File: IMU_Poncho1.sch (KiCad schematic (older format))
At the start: 9 parts, among them J1 Conn_01x06, J2 Conn_01x06_Female, U1 IMU9250

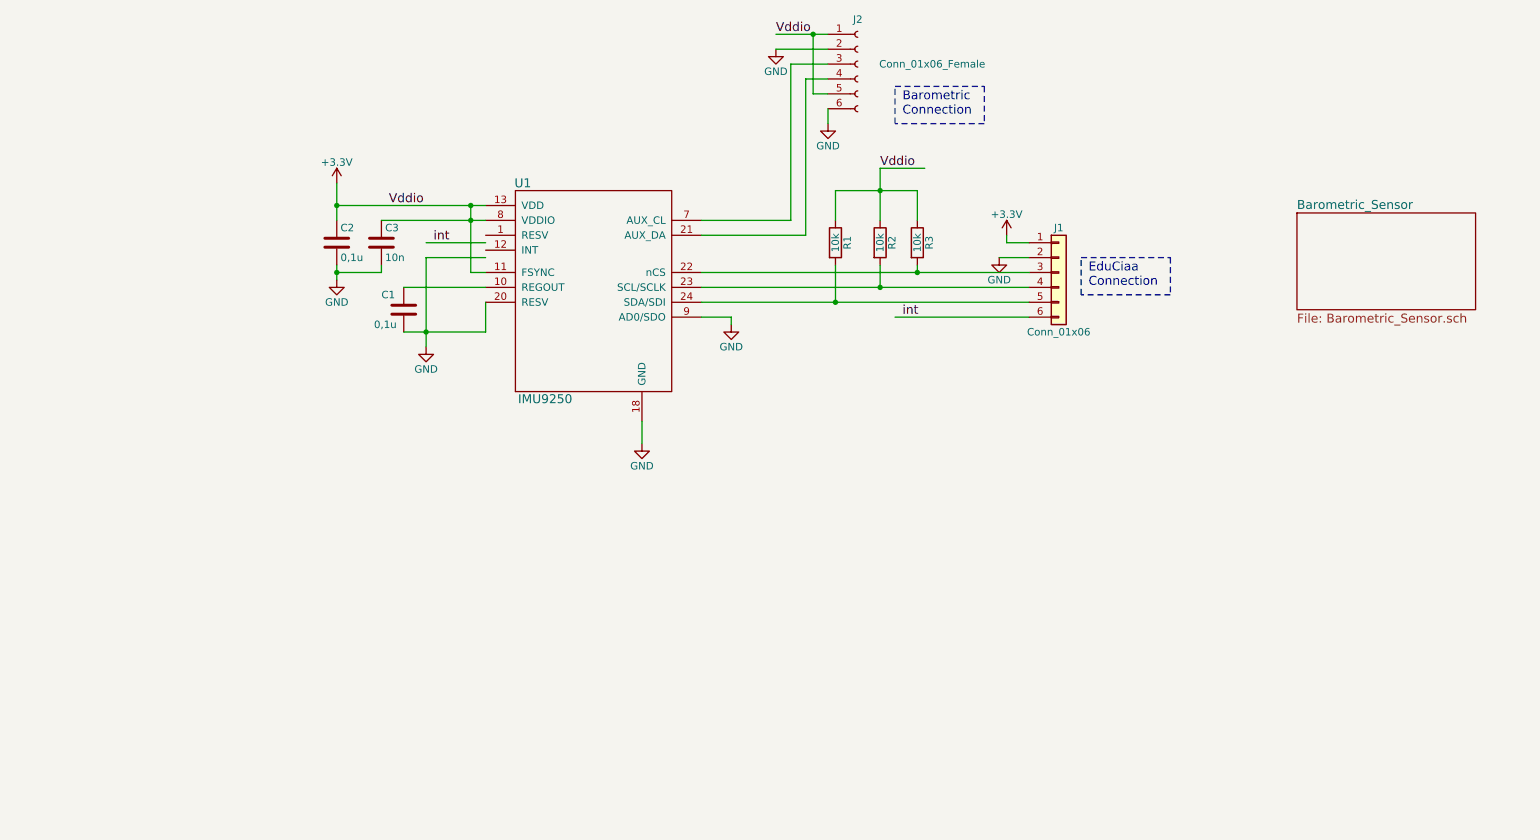
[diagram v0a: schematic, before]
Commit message: Corrigiendo esquematico + datasheets
Detalles de lineas y pines para que no se crucen, +pwr
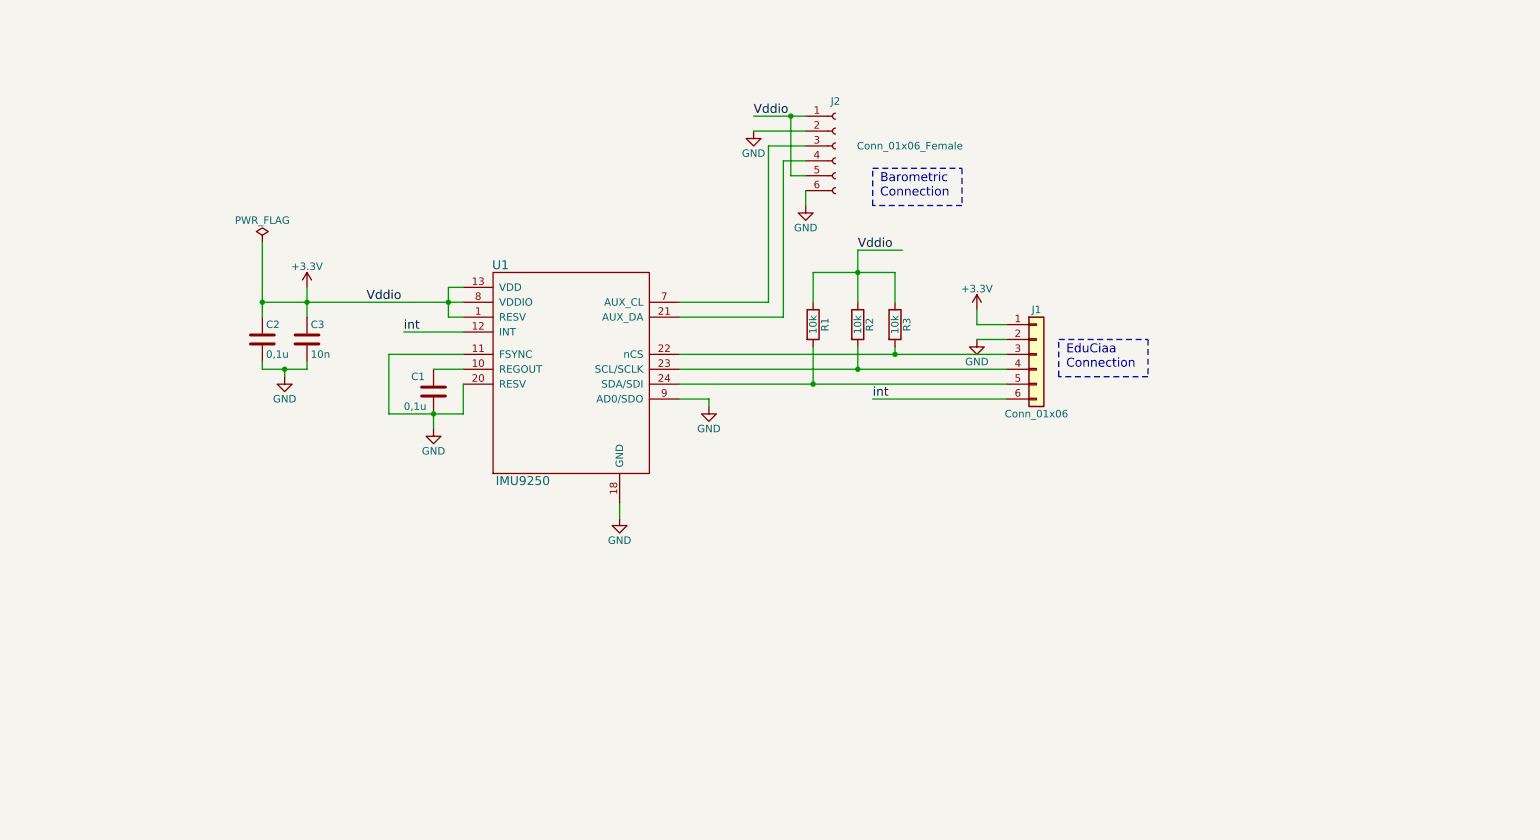
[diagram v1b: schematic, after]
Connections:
- wire segments 43 -> 46
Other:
- moved on the sheet: C1, C2, C3, J1, J2, R1, R2, R3, U1

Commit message: El pcb
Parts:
- removed J1: Conn_01x06, symbol Conn_01x06
- added H1, H2: PCB_HOLE, Poncho_Modelos:Led_Hole, symbol PCB_HOLE
- added XA1: Conn_Poncho2P_2x_20x2, Poncho_Esqueleto:Conn_Poncho_Derecha, symbol Conn_Poncho2P_2x_20x2
- C1: footprint (none) -> Capacitors_SMD:C_0805_HandSoldering; Digikey# (none) -> 478-1395-2-ND; Manf (none) -> AVX; Manf# (none) -> 08055C104KAT2A
- C2: footprint (none) -> Capacitors_SMD:C_0805_HandSoldering; Digikey# (none) -> 08055C104KAT2A; Manf (none) -> AVX; Manf# (none) -> 08055C104KAT2A
- C3: footprint (none) -> Capacitors_SMD:C_0805_HandSoldering; Digikey# (none) -> 311-1136-1-ND; Manf (none) -> Yageo; Manf# (none) -> CC0805KRX7R9BB103
- J1: renamed from J2; footprint (none) -> Poncho_Modelos:bornier6; Digikey# (none) -> 929974E-01-06-ND; Manf (none) -> 3M; Manf# (none) -> 929974-01-06-RK
- R1: footprint (none) -> Resistors_SMD:R_0805_HandSoldering; Digikey# (none) -> CC0805KRX7R9BB103; Manf (none) -> Bourns Inc.; Manf# (none) -> CR0805-JW-103GLF
- R2, R3: footprint (none) -> Resistors_SMD:R_0805_HandSoldering; Digikey# (none) -> CR0805-JW-103GLF-ND; Manf (none) -> Bourns Inc.; Manf# (none) -> CR0805-JW-103GLF
- U1: value IMU9250 -> MPU-9250; footprint (none) -> Housings_DFN_QFN:QFN-24_3x3mm_Pitch0.4mm_NoMask; Digikey# (none) -> 1428-1019-1-ND; Manf (none) -> TDK InvenSense; Manf# (none) -> MPU-9250
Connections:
- net +3V3: now also XA1.1 (+3.3V)
- net GND: now also XA1.20 (GND), XA1.22 (GND), XA1.24 (GND), XA1.26 (GND), XA1.28 (GND), XA1.30 (GND), XA1.32 (GND), XA1.38 (GND), XA1.40 (GND)
- net int: now also XA1.25 (rs232TXD)
- net nCS: now reaches R3.2, U1.22 (nCS)
- net nCS: now also XA1.23 (rs232RXD)
- net at R2.2, U1.23 (SCL/SCLK): now also XA1.21 (i2cSCL)
- net at R1.2, U1.24 (SDA/SDI): now also XA1.19 (i2cSDA)
- no-connect marks 0 -> 28
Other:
- note added: "Agujeros para vizualizar los\nLEDs de la placa EduCIAA"
- moved on the sheet: R1

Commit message: Corrigiendo seguimiento de archivos, borrando del grupo
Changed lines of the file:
@@
 NoConn ~ 2450 6050
 NoConn ~ 3000 6050
+$Comp
+L LOGO #G?
+U 1 1 5A187136
+P 1200 7000
+F 0 "#G?" H 1200 6597 60  0001 C CNN
+F 1 "LOGO" H 1200 7403 60  0001 C CNN
+F 2 "" H 1200 7000 60  0000 C CNN
+F 3 "" H 1200 7000 60  0000 C CNN
+	1    1200 7000
+	1    0    0    -1
+$EndComp
+$Comp
+L Logo_Poncho #G?
+U 1 1 5A187181
+P 2300 7000
+F 0 "#G?" H 2250 6600 60  0001 C CNN
+F 1 "Logo_Poncho" H 2500 6600 60  0001 C CNN
+F 2 "" H 2300 7000 60  0000 C CNN
+F 3 "" H 2300 7000 60  0000 C CNN
+	1    2300 7000
+	1    0    0    -1
+$EndComp
+$Comp
+L OSHWA #G?
+U 1 1 5A1871D7
+P 3100 7050
+F 0 "#G?" H 3070 7450 60  0001 C CNN
+F 1 "OSHWA" H 3100 7353 60  0001 C CNN
+F 2 "" H 3100 7050 60  0000 C CNN
+F 3 "" H 3100 7050 60  0000 C CNN
+	1    3100 7050
+	1    0    0    -1
+$EndComp
 $EndSCHEMATC
